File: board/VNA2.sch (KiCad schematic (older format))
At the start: 61 parts, among them U2 LM339, U3 SA612, U4 SA612, U5 SA612, U6 LM358, U7 LM358

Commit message: Increased isolation between ports
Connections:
- removed net CLK1: C20.2, C21.2, C24.2
- new net CLK1A: C21.2
- new net CLK1B: C20.2
- new net CLK1C: C24.2
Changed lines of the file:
@@
 $EndComp
 $Comp
-L GND #PWR58
+L GND #PWR60
 U 1 1 5BB32DBE
 P 3150 950
-F 0 "#PWR58" H 3150 700 50  0001 C CNN
+F 0 "#PWR60" H 3150 700 50  0001 C CNN
 F 1 "GND" H 3150 800 50  0000 C CNN
 F 2 "" H 3150 950 50  0001 C CNN
@@
 $EndComp
 $Comp
-L GND #PWR49
+L GND #PWR51
 U 1 1 5BB32DD3
 P 1100 1700
-F 0 "#PWR49" H 1100 1450 50  0001 C CNN
+F 0 "#PWR51" H 1100 1450 50  0001 C CNN
 F 1 "GND" H 1100 1550 50  0000 C CNN
 F 2 "" H 1100 1700 50  0001 C CNN
@@
 $EndComp
 $Comp
-L GND #PWR52
+L GND #PWR54
 U 1 1 5BB32DD9
 P 1500 1800
-F 0 "#PWR52" H 1500 1550 50  0001 C CNN
+F 0 "#PWR54" H 1500 1550 50  0001 C CNN
 F 1 "GND" H 1500 1650 50  0000 C CNN
 F 2 "" H 1500 1800 50  0001 C CNN
@@
 NoConn ~ 2800 1450
 Text GLabel 3150 1750 0    60   Input ~ 0
-CLK1
+CLK1A
 $Comp
 L C_Small C21
@@
 $EndComp
 $Comp
-L GND #PWR55
+L GND #PWR57
 U 1 1 5BB32DF0
 P 1900 2250
-F 0 "#PWR55" H 1900 2000 50  0001 C CNN
+F 0 "#PWR57" H 1900 2000 50  0001 C CNN
 F 1 "GND" H 1900 2100 50  0000 C CNN
 F 2 "" H 1900 2250 50  0001 C CNN
@@
 $EndComp
 $Comp
-L GND #PWR60
+L GND #PWR62
 U 1 1 5BB32E0B
 P 4350 2450
-F 0 "#PWR60" H 4350 2200 50  0001 C CNN
+F 0 "#PWR62" H 4350 2200 50  0001 C CNN
 F 1 "GND" H 4350 2300 50  0000 C CNN
 F 2 "" H 4350 2450 50  0001 C CNN
@@
 FILT5V
 $Comp
-L GND #PWR62
+L GND #PWR64
 U 1 1 5BB32E19
 P 4650 1800
-F 0 "#PWR62" H 4650 1550 50  0001 C CNN
+F 0 "#PWR64" H 4650 1550 50  0001 C CNN
 F 1 "GND" H 4650 1650 50  0000 C CNN
 F 2 "" H 4650 1800 50  0001 C CNN
@@
 $EndComp
 $Comp
-L GND #PWR57
+L GND #PWR59
 U 1 1 5BB32E52
 P 3100 2750
-F 0 "#PWR57" H 3100 2500 50  0001 C CNN
+F 0 "#PWR59" H 3100 2500 50  0001 C CNN
 F 1 "GND" H 3100 2600 50  0000 C CNN
 F 2 "" H 3100 2750 50  0001 C CNN
@@
 $EndComp
 $Comp
-L GND #PWR48
+L GND #PWR50
 U 1 1 5BB32E67
 P 1050 3500
-F 0 "#PWR48" H 1050 3250 50  0001 C CNN
+F 0 "#PWR50" H 1050 3250 50  0001 C CNN
 F 1 "GND" H 1050 3350 50  0000 C CNN
 F 2 "" H 1050 3500 50  0001 C CNN
@@
 $EndComp
 $Comp
-L GND #PWR51
+L GND #PWR53
 U 1 1 5BB32E6D
 P 1450 3600
-F 0 "#PWR51" H 1450 3350 50  0001 C CNN
+F 0 "#PWR53" H 1450 3350 50  0001 C CNN
 F 1 "GND" H 1450 3450 50  0000 C CNN
 F 2 "" H 1450 3600 50  0001 C CNN
@@
 NoConn ~ 2750 3250
 Text GLabel 3100 3550 0    60   Input ~ 0
-CLK1
+CLK1B
 $Comp
 L C_Small C20
@@
 $EndComp
 $Comp
-L GND #PWR54
+L GND #PWR56
 U 1 1 5BB32E84
 P 1850 4050
-F 0 "#PWR54" H 1850 3800 50  0001 C CNN
+F 0 "#PWR56" H 1850 3800 50  0001 C CNN
 F 1 "GND" H 1850 3900 50  0000 C CNN
 F 2 "" H 1850 4050 50  0001 C CNN
@@
 $EndComp
 $Comp
-L GND #PWR64
+L GND #PWR66
 U 1 1 5BB32ED8
 P 5700 2600
-F 0 "#PWR64" H 5700 2350 50  0001 C CNN
+F 0 "#PWR66" H 5700 2350 50  0001 C CNN
 F 1 "GND" H 5700 2450 50  0000 C CNN
 F 2 "" H 5700 2600 50  0001 C CNN
@@
 $EndComp
 $Comp
-L GND #PWR66
+L GND #PWR68
 U 1 1 5BB32EE5
 P 6000 2600
-F 0 "#PWR66" H 6000 2350 50  0001 C CNN
+F 0 "#PWR68" H 6000 2350 50  0001 C CNN
 F 1 "GND" H 6000 2450 50  0000 C CNN
 F 2 "" H 6000 2600 50  0001 C CNN
@@
 $EndComp
 $Comp
-L GND #PWR68
+L GND #PWR70
 U 1 1 5BB32EFA
 P 6200 3650
-F 0 "#PWR68" H 6200 3400 50  0001 C CNN
+F 0 "#PWR70" H 6200 3400 50  0001 C CNN
 F 1 "GND" H 6200 3500 50  0000 C CNN
 F 2 "" H 6200 3650 50  0001 C CNN
@@
 $EndComp
 $Comp
-L GND #PWR69
+L GND #PWR71
 U 1 1 5BB32F07
 P 6500 3650
-F 0 "#PWR69" H 6500 3400 50  0001 C CNN
+F 0 "#PWR71" H 6500 3400 50  0001 C CNN
 F 1 "GND" H 6500 3500 50  0000 C CNN
 F 2 "" H 6500 3650 50  0001 C CNN
@@
 $EndComp
 $Comp
-L GND #PWR59
+L GND #PWR61
 U 1 1 5BB496C5
 P 3300 4800
-F 0 "#PWR59" H 3300 4550 50  0001 C CNN
+F 0 "#PWR61" H 3300 4550 50  0001 C CNN
 F 1 "GND" H 3300 4650 50  0000 C CNN
 F 2 "" H 3300 4800 50  0001 C CNN
@@
 $EndComp
 $Comp
-L GND #PWR50
+L GND #PWR52
 U 1 1 5BB496D8
 P 1250 5550
-F 0 "#PWR50" H 1250 5300 50  0001 C CNN
+F 0 "#PWR52" H 1250 5300 50  0001 C CNN
 F 1 "GND" H 1250 5400 50  0000 C CNN
 F 2 "" H 1250 5550 50  0001 C CNN
@@
 $EndComp
 $Comp
-L GND #PWR53
+L GND #PWR55
 U 1 1 5BB496DE
 P 1650 5650
-F 0 "#PWR53" H 1650 5400 50  0001 C CNN
+F 0 "#PWR55" H 1650 5400 50  0001 C CNN
 F 1 "GND" H 1650 5500 50  0000 C CNN
 F 2 "" H 1650 5650 50  0001 C CNN
@@
 NoConn ~ 2950 5300
 Text GLabel 3300 5600 0    60   Input ~ 0
-CLK1
+CLK1C
 $Comp
 L C_Small C24
@@
 $EndComp
 $Comp
-L GND #PWR56
+L GND #PWR58
 U 1 1 5BB496F3
 P 2050 6100
-F 0 "#PWR56" H 2050 5850 50  0001 C CNN
+F 0 "#PWR58" H 2050 5850 50  0001 C CNN
 F 1 "GND" H 2050 5950 50  0000 C CNN
 F 2 "" H 2050 6100 50  0001 C CNN
@@
 $EndComp
 $Comp
-L GND #PWR61
+L GND #PWR63
 U 1 1 5BB4970B
 P 4500 6300
-F 0 "#PWR61" H 4500 6050 50  0001 C CNN
+F 0 "#PWR63" H 4500 6050 50  0001 C CNN
 F 1 "GND" H 4500 6150 50  0000 C CNN
 F 2 "" H 4500 6300 50  0001 C CNN
@@
 FILT5V
 $Comp
-L GND #PWR63
+L GND #PWR65
 U 1 1 5BB49718
 P 4800 5650
-F 0 "#PWR63" H 4800 5400 50  0001 C CNN
+F 0 "#PWR65" H 4800 5400 50  0001 C CNN
 F 1 "GND" H 4800 5500 50  0000 C CNN
 F 2 "" H 4800 5650 50  0001 C CNN
@@
 $EndComp
 $Comp
-L GND #PWR65
+L GND #PWR67
 U 1 1 5BB4974C
 P 5850 6450
-F 0 "#PWR65" H 5850 6200 50  0001 C CNN
+F 0 "#PWR67" H 5850 6200 50  0001 C CNN
 F 1 "GND" H 5850 6300 50  0000 C CNN
 F 2 "" H 5850 6450 50  0001 C CNN
@@
 $EndComp
 $Comp
-L GND #PWR67
+L GND #PWR69
 U 1 1 5BB49758
 P 6150 6450
-F 0 "#PWR67" H 6150 6200 50  0001 C CNN
+F 0 "#PWR69" H 6150 6200 50  0001 C CNN
 F 1 "GND" H 6150 6300 50  0000 C CNN
 F 2 "" H 6150 6450 50  0001 C CNN
@@
 $EndComp
 $Comp
-L GND #PWR70
+L GND #PWR72
 U 1 1 5BB4F877
 P 6700 1650
-F 0 "#PWR70" H 6700 1400 50  0001 C CNN
+F 0 "#PWR72" H 6700 1400 50  0001 C CNN
 F 1 "GND" H 6700 1500 50  0000 C CNN
 F 2 "" H 6700 1650 50  0001 C CNN
@@
 Connection ~ 8850 1100
 $Comp
-L GND #PWR72
+L GND #PWR74
 U 1 1 5BF2333C
 P 8550 850
-F 0 "#PWR72" H 8550 600 50  0001 C CNN
+F 0 "#PWR74" H 8550 600 50  0001 C CNN
 F 1 "GND" H 8550 700 50  0000 C CNN
 F 2 "" H 8550 850 50  0001 C CNN
@@
 	8550 850  8800 850
 $Comp
-L GND #PWR74
+L GND #PWR76
 U 1 1 5BF23614
 P 8850 2000
-F 0 "#PWR74" H 8850 1750 50  0001 C CNN
+F 0 "#PWR76" H 8850 1750 50  0001 C CNN
 F 1 "GND" H 8850 1850 50  0000 C CNN
 F 2 "" H 8850 2000 50  0001 C CNN
@@
 	8850 1900 8850 2000
 $Comp
-L GND #PWR73
+L GND #PWR75
 U 1 1 5BF238FB
 P 8550 1900
-F 0 "#PWR73" H 8550 1650 50  0001 C CNN
+F 0 "#PWR75" H 8550 1650 50  0001 C CNN
 F 1 "GND" H 8550 1750 50  0000 C CNN
 F 2 "" H 8550 1900 50  0001 C CNN
@@
 	8450 2500 8650 2500
 $Comp
-L GND #PWR71
+L GND #PWR73
 U 1 1 5BF23F5D
 P 8500 2800
-F 0 "#PWR71" H 8500 2550 50  0001 C CNN
+F 0 "#PWR73" H 8500 2550 50  0001 C CNN
 F 1 "GND" H 8500 2650 50  0000 C CNN
 F 2 "" H 8500 2800 50  0001 C CNN

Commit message: Changed pullup resistors to 10k for less supply noise
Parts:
- R36, R37: value 1k -> 10k
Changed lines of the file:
@@
 P 7750 3250
 F 0 "R36" V 7830 3250 50  0000 C CNN
-F 1 "1k" V 7750 3250 50  0000 C CNN
+F 1 "10k" V 7750 3250 50  0000 C CNN
 F 2 "Resistors_THT:R_Axial_DIN0207_L6.3mm_D2.5mm_P7.62mm_Horizontal" V 7680 3250 50  0001 C CNN
 F 3 "" H 7750 3250 50  0001 C CNN
@@
 P 7800 4300
 F 0 "R37" V 7880 4300 50  0000 C CNN
-F 1 "1k" V 7800 4300 50  0000 C CNN
+F 1 "10k" V 7800 4300 50  0000 C CNN
 F 2 "Resistors_THT:R_Axial_DIN0207_L6.3mm_D2.5mm_P7.62mm_Horizontal" V 7730 4300 50  0001 C CNN
 F 3 "" H 7800 4300 50  0001 C CNN

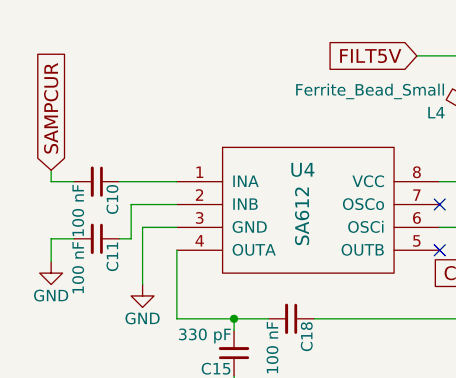
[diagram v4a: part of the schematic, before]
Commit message: Changed to resistive bridge
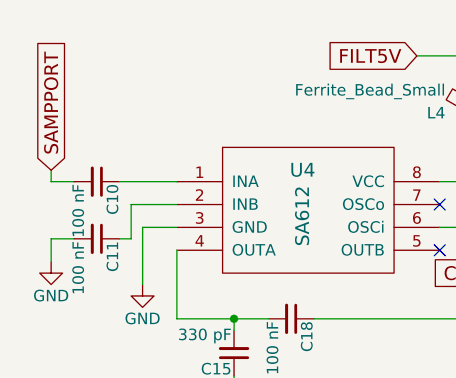
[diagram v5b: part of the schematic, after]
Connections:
- net SAMPCUR renamed SAMPPORT
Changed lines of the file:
@@
 $EndComp
 $Comp
-L GND #PWR057
+L GND #PWR69
 U 1 1 5BB32DBE
 P 3150 950
-F 0 "#PWR057" H 3150 700 50  0001 C CNN
+F 0 "#PWR69" H 3150 700 50  0001 C CNN
 F 1 "GND" H 3150 800 50  0000 C CNN
 F 2 "" H 3150 950 50  0001 C CNN
@@
 $EndComp
 Text GLabel 1100 1300 1    60   Input ~ 0
-SAMPCUR
+SAMPPORT
 $Comp
 L C_Small C10
@@
 $EndComp
 $Comp
-L GND #PWR058
+L GND #PWR60
 U 1 1 5BB32DD3
 P 1100 1700
-F 0 "#PWR058" H 1100 1450 50  0001 C CNN
+F 0 "#PWR60" H 1100 1450 50  0001 C CNN
 F 1 "GND" H 1100 1550 50  0000 C CNN
 F 2 "" H 1100 1700 50  0001 C CNN
@@
 $EndComp
 $Comp
-L GND #PWR059
+L GND #PWR63
 U 1 1 5BB32DD9
 P 1500 1800
-F 0 "#PWR059" H 1500 1550 50  0001 C CNN
+F 0 "#PWR63" H 1500 1550 50  0001 C CNN
 F 1 "GND" H 1500 1650 50  0000 C CNN
 F 2 "" H 1500 1800 50  0001 C CNN
@@
 $EndComp
 $Comp
-L GND #PWR060
+L GND #PWR66
 U 1 1 5BB32DF0
 P 1900 2250
-F 0 "#PWR060" H 1900 2000 50  0001 C CNN
+F 0 "#PWR66" H 1900 2000 50  0001 C CNN
 F 1 "GND" H 1900 2100 50  0000 C CNN
 F 2 "" H 1900 2250 50  0001 C CNN
@@
 $EndComp
 $Comp
-L GND #PWR061
+L GND #PWR71
 U 1 1 5BB32E0B
 P 4350 2450
-F 0 "#PWR061" H 4350 2200 50  0001 C CNN
+F 0 "#PWR71" H 4350 2200 50  0001 C CNN
 F 1 "GND" H 4350 2300 50  0000 C CNN
 F 2 "" H 4350 2450 50  0001 C CNN
@@
 FILT5V
 $Comp
-L GND #PWR062
+L GND #PWR73
 U 1 1 5BB32E19
 P 4650 1800
-F 0 "#PWR062" H 4650 1550 50  0001 C CNN
+F 0 "#PWR73" H 4650 1550 50  0001 C CNN
 F 1 "GND" H 4650 1650 50  0000 C CNN
 F 2 "" H 4650 1800 50  0001 C CNN
@@
 $EndComp
 $Comp
-L GND #PWR063
+L GND #PWR68
 U 1 1 5BB32E52
 P 3100 2750
-F 0 "#PWR063" H 3100 2500 50  0001 C CNN
+F 0 "#PWR68" H 3100 2500 50  0001 C CNN
 F 1 "GND" H 3100 2600 50  0000 C CNN
 F 2 "" H 3100 2750 50  0001 C CNN
@@
 $EndComp
 $Comp
-L GND #PWR064
+L GND #PWR59
 U 1 1 5BB32E67
 P 1050 3500
-F 0 "#PWR064" H 1050 3250 50  0001 C CNN
+F 0 "#PWR59" H 1050 3250 50  0001 C CNN
 F 1 "GND" H 1050 3350 50  0000 C CNN
 F 2 "" H 1050 3500 50  0001 C CNN
@@
 $EndComp
 $Comp
-L GND #PWR065
+L GND #PWR62
 U 1 1 5BB32E6D
 P 1450 3600
-F 0 "#PWR065" H 1450 3350 50  0001 C CNN
+F 0 "#PWR62" H 1450 3350 50  0001 C CNN
 F 1 "GND" H 1450 3450 50  0000 C CNN
 F 2 "" H 1450 3600 50  0001 C CNN
@@
 $EndComp
 $Comp
-L GND #PWR066
+L GND #PWR65
 U 1 1 5BB32E84
 P 1850 4050
-F 0 "#PWR066" H 1850 3800 50  0001 C CNN
+F 0 "#PWR65" H 1850 3800 50  0001 C CNN
 F 1 "GND" H 1850 3900 50  0000 C CNN
 F 2 "" H 1850 4050 50  0001 C CNN
@@
 $EndComp
 $Comp
-L GND #PWR067
+L GND #PWR75
 U 1 1 5BB32ED8
 P 5700 2600
-F 0 "#PWR067" H 5700 2350 50  0001 C CNN
+F 0 "#PWR75" H 5700 2350 50  0001 C CNN
 F 1 "GND" H 5700 2450 50  0000 C CNN
 F 2 "" H 5700 2600 50  0001 C CNN
@@
 $EndComp
 $Comp
-L GND #PWR068
+L GND #PWR77
 U 1 1 5BB32EE5
 P 6000 2600
-F 0 "#PWR068" H 6000 2350 50  0001 C CNN
+F 0 "#PWR77" H 6000 2350 50  0001 C CNN
 F 1 "GND" H 6000 2450 50  0000 C CNN
 F 2 "" H 6000 2600 50  0001 C CNN
@@
 $EndComp
 $Comp
-L GND #PWR069
+L GND #PWR79
 U 1 1 5BB32EFA
 P 6200 3650
-F 0 "#PWR069" H 6200 3400 50  0001 C CNN
+F 0 "#PWR79" H 6200 3400 50  0001 C CNN
 F 1 "GND" H 6200 3500 50  0000 C CNN
 F 2 "" H 6200 3650 50  0001 C CNN
@@
 $EndComp
 $Comp
-L GND #PWR070
+L GND #PWR80
 U 1 1 5BB32F07
 P 6500 3650
-F 0 "#PWR070" H 6500 3400 50  0001 C CNN
+F 0 "#PWR80" H 6500 3400 50  0001 C CNN
 F 1 "GND" H 6500 3500 50  0000 C CNN
 F 2 "" H 6500 3650 50  0001 C CNN
@@
 $EndComp
 $Comp
-L GND #PWR071
+L GND #PWR70
 U 1 1 5BB496C5
 P 3300 4800
-F 0 "#PWR071" H 3300 4550 50  0001 C CNN
+F 0 "#PWR70" H 3300 4550 50  0001 C CNN
 F 1 "GND" H 3300 4650 50  0000 C CNN
 F 2 "" H 3300 4800 50  0001 C CNN
@@
 $EndComp
 $Comp
-L GND #PWR072
+L GND #PWR61
 U 1 1 5BB496D8
 P 1250 5550
-F 0 "#PWR072" H 1250 5300 50  0001 C CNN
+F 0 "#PWR61" H 1250 5300 50  0001 C CNN
 F 1 "GND" H 1250 5400 50  0000 C CNN
 F 2 "" H 1250 5550 50  0001 C CNN
@@
 $EndComp
 $Comp
-L GND #PWR073
+L GND #PWR64
 U 1 1 5BB496DE
 P 1650 5650
-F 0 "#PWR073" H 1650 5400 50  0001 C CNN
+F 0 "#PWR64" H 1650 5400 50  0001 C CNN
 F 1 "GND" H 1650 5500 50  0000 C CNN
 F 2 "" H 1650 5650 50  0001 C CNN
@@
 $EndComp
 $Comp
-L GND #PWR074
+L GND #PWR67
 U 1 1 5BB496F3
 P 2050 6100
-F 0 "#PWR074" H 2050 5850 50  0001 C CNN
+F 0 "#PWR67" H 2050 5850 50  0001 C CNN
 F 1 "GND" H 2050 5950 50  0000 C CNN
 F 2 "" H 2050 6100 50  0001 C CNN
@@
 $EndComp
 $Comp
-L GND #PWR075
+L GND #PWR72
 U 1 1 5BB4970B
 P 4500 6300
-F 0 "#PWR075" H 4500 6050 50  0001 C CNN
+F 0 "#PWR72" H 4500 6050 50  0001 C CNN
 F 1 "GND" H 4500 6150 50  0000 C CNN
 F 2 "" H 4500 6300 50  0001 C CNN
@@
 FILT5V
 $Comp
-L GND #PWR076
+L GND #PWR74
 U 1 1 5BB49718
 P 4800 5650
-F 0 "#PWR076" H 4800 5400 50  0001 C CNN
+F 0 "#PWR74" H 4800 5400 50  0001 C CNN
 F 1 "GND" H 4800 5500 50  0000 C CNN
 F 2 "" H 4800 5650 50  0001 C CNN
@@
 $EndComp
 $Comp
-L GND #PWR077
+L GND #PWR76
 U 1 1 5BB4974C
 P 5850 6450
-F 0 "#PWR077" H 5850 6200 50  0001 C CNN
+F 0 "#PWR76" H 5850 6200 50  0001 C CNN
 F 1 "GND" H 5850 6300 50  0000 C CNN
 F 2 "" H 5850 6450 50  0001 C CNN
@@
 $EndComp
 $Comp
-L GND #PWR078
+L GND #PWR78
 U 1 1 5BB49758
 P 6150 6450
-F 0 "#PWR078" H 6150 6200 50  0001 C CNN
+F 0 "#PWR78" H 6150 6200 50  0001 C CNN
 F 1 "GND" H 6150 6300 50  0000 C CNN
 F 2 "" H 6150 6450 50  0001 C CNN
@@
 $EndComp
 $Comp
-L GND #PWR079
+L GND #PWR81
 U 1 1 5BB4F877
 P 6700 1650
-F 0 "#PWR079" H 6700 1400 50  0001 C CNN
+F 0 "#PWR81" H 6700 1400 50  0001 C CNN
 F 1 "GND" H 6700 1500 50  0000 C CNN
 F 2 "" H 6700 1650 50  0001 C CNN
@@
 Connection ~ 8850 1100
 $Comp
-L GND #PWR080
+L GND #PWR83
 U 1 1 5BF2333C
 P 8550 850
-F 0 "#PWR080" H 8550 600 50  0001 C CNN
+F 0 "#PWR83" H 8550 600 50  0001 C CNN
 F 1 "GND" H 8550 700 50  0000 C CNN
 F 2 "" H 8550 850 50  0001 C CNN
@@
 	8550 850  8800 850
 $Comp
-L GND #PWR081
+L GND #PWR85
 U 1 1 5BF23614
 P 8850 2000
-F 0 "#PWR081" H 8850 1750 50  0001 C CNN
+F 0 "#PWR85" H 8850 1750 50  0001 C CNN
 F 1 "GND" H 8850 1850 50  0000 C CNN
 F 2 "" H 8850 2000 50  0001 C CNN
@@
 	8850 1900 8850 2000
 $Comp
-L GND #PWR082
+L GND #PWR84
 U 1 1 5BF238FB
 P 8550 1900
-F 0 "#PWR082" H 8550 1650 50  0001 C CNN
+F 0 "#PWR84" H 8550 1650 50  0001 C CNN
 F 1 "GND" H 8550 1750 50  0000 C CNN
 F 2 "" H 8550 1900 50  0001 C CNN
@@
 	8450 2500 8650 2500
 $Comp
-L GND #PWR083
+L GND #PWR82
 U 1 1 5BF23F5D
 P 8500 2800
-F 0 "#PWR083" H 8500 2550 50  0001 C CNN
+F 0 "#PWR82" H 8500 2550 50  0001 C CNN
 F 1 "GND" H 8500 2650 50  0000 C CNN
 F 2 "" H 8500 2800 50  0001 C CNN
